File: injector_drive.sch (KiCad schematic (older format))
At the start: 10 parts

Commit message: Corrected ERC errors by fixing the custom FreeEMS components pinouts
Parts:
- removed R?: 1k, R4-SM0805, symbol R
- added R124: 1k, R4-SM0805, symbol R
- gave numbers to parts that had none: 9
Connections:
- net inductive_power_drive: now also R124.2
- net at U15.1 (IN): now also R124.1
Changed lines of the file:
@@
-EESchema Schematic File Version 2  date Sat 03 Jul 2010 10:49:02 AM ART
+EESchema Schematic File Version 2  date Sat 03 Jul 2010 12:32:24 PM ART
 LIBS:power
 LIBS:freeEMS_lib
@@
 Rsense MUST BE KELVIN CONNECTED TO THE DEVICE PINS
 $Comp
-L GND #PWR?
+L GND #PWR021
 U 1 1 4C2ED38A
 P 6600 2750
-AR Path="/4C2F3BE4/4C2ED38A" Ref="#PWR?"  Part="1"
-AR Path="/4C2F3DD9/4C2ED38A" Ref="#PWR?"  Part="1"
-F 0 "#PWR?" H 6600 2750 30  0001 C CNN
+AR Path="/4C2F3E4C/4C2ED38A" Ref="#PWR021"  Part="1"
+AR Path="/4C2F3E39/4C2ED38A" Ref="#PWR024"  Part="1"
+AR Path="/4C2F3E27/4C2ED38A" Ref="#PWR027"  Part="1"
+AR Path="/4C2F3E07/4C2ED38A" Ref="#PWR030"  Part="1"
+AR Path="/4C2F3DD9/4C2ED38A" Ref="#PWR033"  Part="1"
+AR Path="/4C2F3BE4/4C2ED38A" Ref="#PWR036"  Part="1"
+F 0 "#PWR036" H 6600 2750 30  0001 C CNN
 F 1 "GND" H 6600 2680 30  0001 C CNN
 	1    6600 2750
@@
 $EndComp
 $Comp
-L GND #PWR?
+L GND #PWR022
 U 1 1 4C2ED35A
 P 5950 3650
-AR Path="/4C2F3BE4/4C2ED35A" Ref="#PWR?"  Part="1"
-AR Path="/4C2F3DD9/4C2ED35A" Ref="#PWR?"  Part="1"
-F 0 "#PWR?" H 5950 3650 30  0001 C CNN
+AR Path="/4C2F3E4C/4C2ED35A" Ref="#PWR022"  Part="1"
+AR Path="/4C2F3E39/4C2ED35A" Ref="#PWR025"  Part="1"
+AR Path="/4C2F3E27/4C2ED35A" Ref="#PWR028"  Part="1"
+AR Path="/4C2F3E07/4C2ED35A" Ref="#PWR031"  Part="1"
+AR Path="/4C2F3DD9/4C2ED35A" Ref="#PWR034"  Part="1"
+AR Path="/4C2F3BE4/4C2ED35A" Ref="#PWR037"  Part="1"
+F 0 "#PWR037" H 5950 3650 30  0001 C CNN
 F 1 "GND" H 5950 3580 30  0001 C CNN
 	1    5950 3650
@@
 $EndComp
 $Comp
-L GND #PWR?
+L GND #PWR023
 U 1 1 4C2ED354
 P 6100 3000
-AR Path="/4C2F3BE4/4C2ED354" Ref="#PWR?"  Part="1"
-AR Path="/4C2F3DD9/4C2ED354" Ref="#PWR?"  Part="1"
-F 0 "#PWR?" H 6100 3000 30  0001 C CNN
+AR Path="/4C2F3E4C/4C2ED354" Ref="#PWR023"  Part="1"
+AR Path="/4C2F3E39/4C2ED354" Ref="#PWR026"  Part="1"
+AR Path="/4C2F3E27/4C2ED354" Ref="#PWR029"  Part="1"
+AR Path="/4C2F3E07/4C2ED354" Ref="#PWR032"  Part="1"
+AR Path="/4C2F3DD9/4C2ED354" Ref="#PWR035"  Part="1"
+AR Path="/4C2F3BE4/4C2ED354" Ref="#PWR038"  Part="1"
+F 0 "#PWR038" H 6100 3000 30  0001 C CNN
 F 1 "GND" H 6100 2930 30  0001 C CNN
 	1    6100 3000
@@
 $EndComp
 $Comp
-L C C?
+L C C59
 U 1 1 4C2ED144
 P 6600 2550
-AR Path="/4C2F3BE4/4C2ED144" Ref="C?"  Part="1"
-AR Path="/4C2F3DD9/4C2ED144" Ref="C?"  Part="1"
-F 0 "C?" H 6650 2650 50  0000 L CNN
+AR Path="/4C2F3E4C/4C2ED144" Ref="C59"  Part="1"
+AR Path="/4C2F3E39/4C2ED144" Ref="C57"  Part="1"
+AR Path="/4C2F3E27/4C2ED144" Ref="C55"  Part="1"
+AR Path="/4C2F3E07/4C2ED144" Ref="C53"  Part="1"
+AR Path="/4C2F3DD9/4C2ED144" Ref="C51"  Part="1"
+AR Path="/4C2F3BE4/4C2ED144" Ref="C49"  Part="1"
+F 0 "C59" H 6650 2650 50  0000 L CNN
 F 1 "1uF" H 6650 2450 50  0000 L CNN
 	1    6600 2550
@@
 $EndComp
 $Comp
-L R R?
+L R R126
 U 1 1 4C2ED135
 P 6250 2550
-AR Path="/4C2F3BE4/4C2ED135" Ref="R?"  Part="1"
-AR Path="/4C2F3DD9/4C2ED135" Ref="R?"  Part="1"
-F 0 "R?" V 6330 2550 50  0000 C CNN
+AR Path="/4C2F3E4C/4C2ED135" Ref="R126"  Part="1"
+AR Path="/4C2F3E39/4C2ED135" Ref="R123"  Part="1"
+AR Path="/4C2F3E27/4C2ED135" Ref="R120"  Part="1"
+AR Path="/4C2F3E07/4C2ED135" Ref="R117"  Part="1"
+AR Path="/4C2F3DD9/4C2ED135" Ref="R114"  Part="1"
+AR Path="/4C2F3BE4/4C2ED135" Ref="R111"  Part="1"
+F 0 "R126" V 6330 2550 50  0000 C CNN
 F 1 "3.9k" V 6250 2550 50  0000 C CNN
 	1    6250 2550
@@
 $EndComp
 $Comp
-L ZENER D?
+L ZENER D57
 U 1 1 4C2ED0C2
 P 3150 3150
-AR Path="/4C2F3BE4/4C2ED0C2" Ref="D?"  Part="1"
-AR Path="/4C2F3DD9/4C2ED0C2" Ref="D?"  Part="1"
-F 0 "D?" H 3150 3250 50  0000 C CNN
+AR Path="/4C2F3E4C/4C2ED0C2" Ref="D57"  Part="1"
+AR Path="/4C2F3E39/4C2ED0C2" Ref="D56"  Part="1"
+AR Path="/4C2F3E27/4C2ED0C2" Ref="D55"  Part="1"
+AR Path="/4C2F3E07/4C2ED0C2" Ref="D54"  Part="1"
+AR Path="/4C2F3DD9/4C2ED0C2" Ref="D53"  Part="1"
+AR Path="/4C2F3BE4/4C2ED0C2" Ref="D52"  Part="1"
+F 0 "D57" H 3150 3250 50  0000 C CNN
 F 1 "33v 5w" H 3150 3050 40  0000 C CNN
 	1    3150 3150
@@
 $EndComp
 $Comp
-L R R?
+L R R125
 U 1 1 4C2ED077
 P 5200 3450
-AR Path="/4C2F3BE4/4C2ED077" Ref="R?"  Part="1"
-AR Path="/4C2F3DD9/4C2ED077" Ref="R?"  Part="1"
-F 0 "R?" V 5280 3450 50  0000 C CNN
+AR Path="/4C2F3E4C/4C2ED077" Ref="R125"  Part="1"
+AR Path="/4C2F3E39/4C2ED077" Ref="R122"  Part="1"
+AR Path="/4C2F3E27/4C2ED077" Ref="R119"  Part="1"
+AR Path="/4C2F3E07/4C2ED077" Ref="R116"  Part="1"
+AR Path="/4C2F3DD9/4C2ED077" Ref="R113"  Part="1"
+AR Path="/4C2F3BE4/4C2ED077" Ref="R110"  Part="1"
+F 0 "R125" V 5280 3450 50  0000 C CNN
 F 1 "0.1 2W" V 5200 3450 50  0000 C CNN
 	1    5200 3450
@@
 $EndComp
 $Comp
-L C C?
+L C C58
 U 1 1 4C2ED01B
 P 4150 3000
-AR Path="/4C2F3BE4/4C2ED01B" Ref="C?"  Part="1"
-AR Path="/4C2F3DD9/4C2ED01B" Ref="C?"  Part="1"
-F 0 "C?" H 4200 3100 50  0000 L CNN
+AR Path="/4C2F3E4C/4C2ED01B" Ref="C58"  Part="1"
+AR Path="/4C2F3E39/4C2ED01B" Ref="C56"  Part="1"
+AR Path="/4C2F3E27/4C2ED01B" Ref="C54"  Part="1"
+AR Path="/4C2F3E07/4C2ED01B" Ref="C52"  Part="1"
+AR Path="/4C2F3DD9/4C2ED01B" Ref="C50"  Part="1"
+AR Path="/4C2F3BE4/4C2ED01B" Ref="C48"  Part="1"
+F 0 "C58" H 4200 3100 50  0000 L CNN
 F 1 ".01uF" H 4200 2900 50  0000 L CNN
 	1    4150 3000
@@
 $EndComp
 $Comp
-L DARL_N Q?
+L DARL_N Q17
 U 1 1 4C2ECF62
 P 3600 3200
-AR Path="/4C2F3BE4/4C2ECF62" Ref="Q?"  Part="1"
-AR Path="/4C2F3DD9/4C2ECF62" Ref="Q?"  Part="1"
-F 0 "Q?" H 3600 3450 50  0000 C CNN
+AR Path="/4C2F3E4C/4C2ECF62" Ref="Q17"  Part="1"
+AR Path="/4C2F3E39/4C2ECF62" Ref="Q16"  Part="1"
+AR Path="/4C2F3E27/4C2ECF62" Ref="Q15"  Part="1"
+AR Path="/4C2F3E07/4C2ECF62" Ref="Q14"  Part="1"
+AR Path="/4C2F3DD9/4C2ECF62" Ref="Q13"  Part="1"
+AR Path="/4C2F3BE4/4C2ECF62" Ref="Q12"  Part="1"
+F 0 "Q17" H 3600 3450 50  0000 C CNN
 F 1 "2N6044" H 3400 3100 50  0000 C CNN
 	1    3600 3200
@@
 $EndComp
 $Comp
-L LM1949 U?
+L LM1949 U15
 U 1 1 4C2ECEC5
 P 5150 2850
-AR Path="/4C2F3BE4/4C2ECEC5" Ref="U?"  Part="1"
-AR Path="/4C2F3DD9/4C2ECEC5" Ref="U?"  Part="1"
-F 0 "U?" H 5200 3150 60  0000 C CNN
+AR Path="/4C2F3E4C/4C2ECEC5" Ref="U15"  Part="1"
+AR Path="/4C2F3E39/4C2ECEC5" Ref="U14"  Part="1"
+AR Path="/4C2F3E27/4C2ECEC5" Ref="U13"  Part="1"
+AR Path="/4C2F3E07/4C2ECEC5" Ref="U12"  Part="1"
+AR Path="/4C2F3DD9/4C2ECEC5" Ref="U11"  Part="1"
+AR Path="/4C2F3BE4/4C2ECEC5" Ref="U10"  Part="1"
+F 0 "U15" H 5200 3150 60  0000 C CNN
 F 1 "LM1949" H 5150 2500 60  0000 C CNN
 F 2 "DIP8" H 5260 3210 60  0001 C CNN
@@
 $EndComp
 $Comp
-L CONN_1 P?
+L CONN_1 P55
 U 1 1 48AA1A76
 P 3650 2700
-AR Path="/4C2F3BE4/48AA1A76" Ref="P?"  Part="1"
-AR Path="/4C2F3DD9/48AA1A76" Ref="P?"  Part="1"
-F 0 "P?" H 3730 2700 40  0000 L CNN
+AR Path="/4C2F3E4C/48AA1A76" Ref="P55"  Part="1"
+AR Path="/4C2F3E39/48AA1A76" Ref="P53"  Part="1"
+AR Path="/4C2F3E27/48AA1A76" Ref="P51"  Part="1"
+AR Path="/4C2F3E07/48AA1A76" Ref="P49"  Part="1"
+AR Path="/4C2F3DD9/48AA1A76" Ref="P47"  Part="1"
+AR Path="/4C2F3BE4/48AA1A76" Ref="P45"  Part="1"
+F 0 "P55" H 3730 2700 40  0000 L CNN
 F 1 "CONN_1" H 3650 2755 30  0001 C CNN
 F 2 "1PIN" V -2870 3300 60  0001 C CNN
@@
 $EndComp
 $Comp
-L CONN_1 P?
+L CONN_1 P54
 U 1 1 48AA1A73
 P 3650 2500
-AR Path="/4C2F3BE4/48AA1A73" Ref="P?"  Part="1"
-AR Path="/4C2F3DD9/48AA1A73" Ref="P?"  Part="1"
-F 0 "P?" H 3730 2500 40  0000 L CNN
+AR Path="/4C2F3E4C/48AA1A73" Ref="P54"  Part="1"
+AR Path="/4C2F3E39/48AA1A73" Ref="P52"  Part="1"
+AR Path="/4C2F3E27/48AA1A73" Ref="P50"  Part="1"
+AR Path="/4C2F3E07/48AA1A73" Ref="P48"  Part="1"
+AR Path="/4C2F3DD9/48AA1A73" Ref="P46"  Part="1"
+AR Path="/4C2F3BE4/48AA1A73" Ref="P44"  Part="1"
+F 0 "P54" H 3730 2500 40  0000 L CNN
 F 1 "CONN_1" H 3650 2555 30  0001 C CNN
 F 2 "1PIN" V -2870 3300 60  0001 C CNN
@@
 12v_power
 $Comp
-L R R?
-U 1 1 488A2B3B
+L R R124
+U 1 1 4C2F52D2
 P 3600 2000
-AR Path="/4C2F3BE4/488A2B3B" Ref="R?"  Part="1"
-AR Path="/4C2F3DD9/488A2B3B" Ref="R?"  Part="1"
-F 0 "R?" V 3680 2000 50  0000 C CNN
+AR Path="/4C2F3E4C/4C2F52D2" Ref="R124"  Part="1"
+AR Path="/4C2F3E39/4C2F52D2" Ref="R121"  Part="1"
+AR Path="/4C2F3E27/4C2F52D2" Ref="R118"  Part="1"
+AR Path="/4C2F3E07/4C2F52D2" Ref="R115"  Part="1"
+AR Path="/4C2F3DD9/4C2F52D2" Ref="R112"  Part="1"
+AR Path="/4C2F3BE4/4C2F52D2" Ref="R109"  Part="1"
+F 0 "R124" V 3680 2000 50  0000 C CNN
 F 1 "1k" V 3600 2000 50  0000 C CNN
 F 2 "R4-SM0805" V 3780 2100 60  0001 C CNN

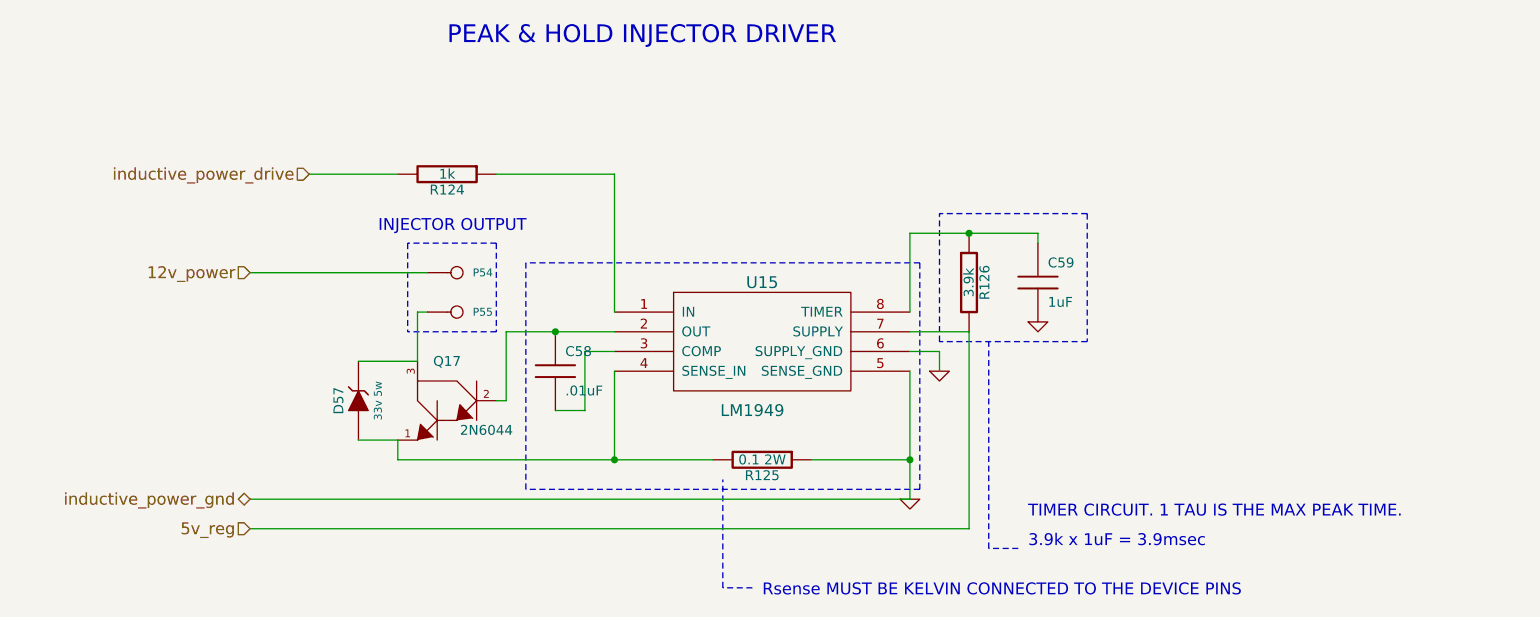
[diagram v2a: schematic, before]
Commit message: PCB redesign. Only P&H is layeed down.
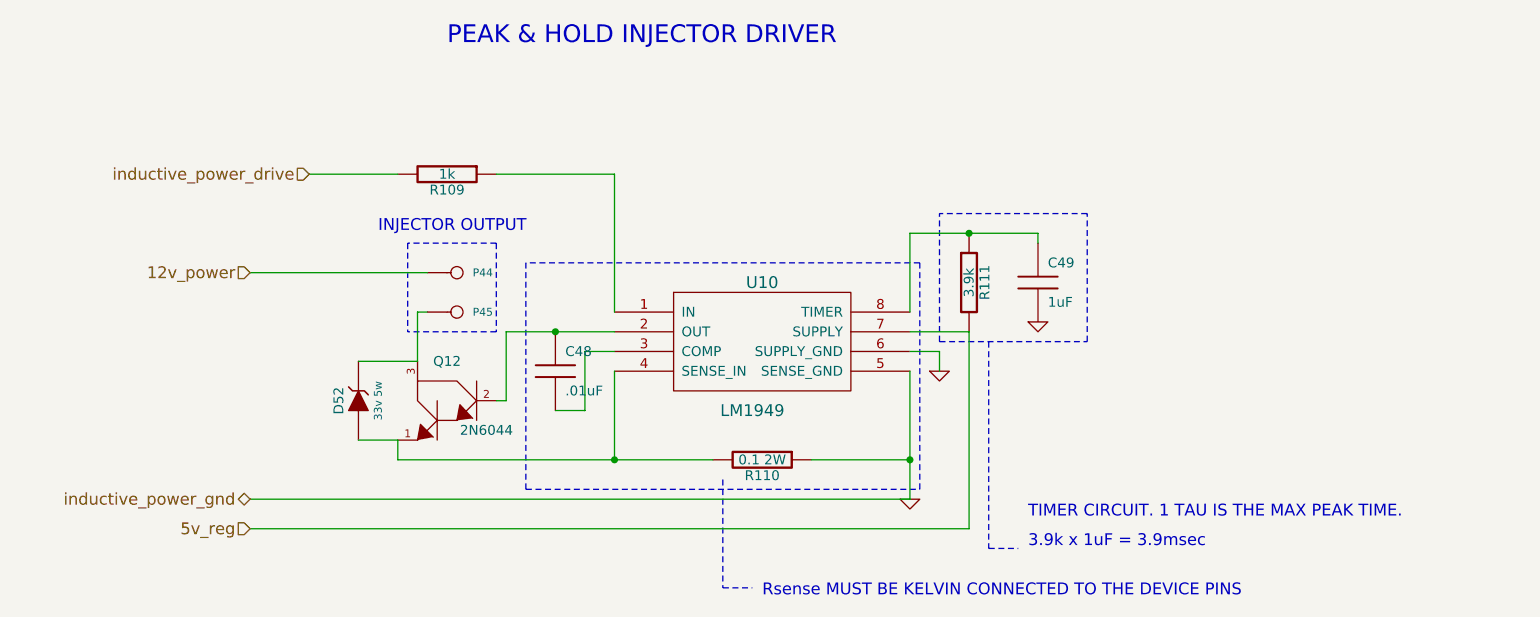
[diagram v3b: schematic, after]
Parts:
- U15: footprint DIP8 -> 8dip300
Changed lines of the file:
@@
-EESchema Schematic File Version 2  date Sat 03 Jul 2010 12:32:24 PM ART
+EESchema Schematic File Version 2  date Sat 03 Jul 2010 05:37:07 PM ART
 LIBS:power
 LIBS:freeEMS_lib
@@
 EELAYER END
 $Descr A4 11700 8267
-Sheet 2 41
+Sheet 7 41
 Title "freeEMS 1.0"
 Date "3 jul 2010"
@@
 Comment4 ""
 $EndDescr
+Wire Wire Line
+	3350 2000 2900 2000
+Wire Notes Line
+	5000 3550 5000 4100
+Wire Notes Line
+	5000 4100 5150 4100
+Wire Notes Line
+	3850 2800 3400 2800
+Wire Notes Line
+	3850 2350 3400 2350
+Wire Notes Line
+	3850 2350 3850 2800
+Wire Notes Line
+	3400 2350 3400 2800
+Wire Wire Line
+	2600 3800 6250 3800
+Wire Wire Line
+	6250 3800 6250 2800
+Wire Wire Line
+	6100 3000 6100 2900
+Wire Wire Line
+	6100 2900 5950 2900
+Connection ~ 6250 2300
+Wire Wire Line
+	6600 2350 6600 2300
+Wire Wire Line
+	6600 2300 5950 2300
+Wire Wire Line
+	4450 2700 4450 2000
+Wire Wire Line
+	4450 2000 3850 2000
+Wire Wire Line
+	2600 2500 3500 2500
+Wire Wire Line
+	3150 2950 3450 2950
+Connection ~ 4450 3450
+Wire Wire Line
+	3350 3450 3350 3350
+Wire Wire Line
+	3350 3450 4950 3450
+Wire Wire Line
+	5450 3450 5950 3450
+Wire Wire Line
+	3900 3150 3900 2800
+Wire Wire Line
+	3900 3150 3850 3150
+Wire Wire Line
+	3900 2800 4450 2800
+Connection ~ 4150 2800
+Wire Wire Line
+	4150 3200 4300 3200
+Wire Wire Line
+	4300 3200 4300 2900
+Wire Wire Line
+	4300 2900 4450 2900
+Wire Wire Line
+	4450 3450 4450 3000
+Wire Wire Line
+	3350 3350 3150 3350
+Wire Wire Line
+	3450 2950 3450 2700
+Wire Wire Line
+	3450 2700 3500 2700
+Wire Wire Line
+	5950 2300 5950 2700
+Wire Wire Line
+	6250 2800 5950 2800
+Wire Wire Line
+	2600 3650 5950 3650
+Wire Wire Line
+	5950 3650 5950 3000
+Connection ~ 5950 3450
+Wire Notes Line
+	6100 2850 6100 2200
+Wire Notes Line
+	6100 2850 6850 2850
+Wire Notes Line
+	6850 2850 6850 2200
+Wire Notes Line
+	6850 2200 6100 2200
+Wire Notes Line
+	4000 3600 4000 2450
+Wire Notes Line
+	4000 3600 6000 3600
+Wire Notes Line
+	6000 3600 6000 2450
+Wire Notes Line
+	6000 2450 4000 2450
+Wire Notes Line
+	6350 2850 6350 3900
+Wire Notes Line
+	6350 3900 6500 3900
 Text Notes 3600 1350 0    90   ~ 0
 PEAK & HOLD INJECTOR DRIVER
@@
 Text Notes 3250 2300 0    60   ~ 0
 INJECTOR OUTPUT
-Wire Notes Line
-	6500 3900 6350 3900
-Wire Notes Line
-	6350 3900 6350 2850
-Wire Notes Line
-	6000 2450 4000 2450
-Wire Notes Line
-	6000 2450 6000 3600
-Wire Notes Line
-	6000 3600 4000 3600
-Wire Notes Line
-	4000 3600 4000 2450
-Wire Notes Line
-	6850 2200 6100 2200
-Wire Notes Line
-	6850 2200 6850 2850
-Wire Notes Line
-	6850 2850 6100 2850
-Wire Notes Line
-	6100 2850 6100 2200
-Connection ~ 5950 3450
-Wire Wire Line
-	5950 3000 5950 3650
-Wire Wire Line
-	5950 3650 2600 3650
-Wire Wire Line
-	5950 2800 6250 2800
-Wire Wire Line
-	5950 2700 5950 2300
-Wire Wire Line
-	2900 2000 3350 2000
-Wire Wire Line
-	3500 2700 3450 2700
-Wire Wire Line
-	3450 2700 3450 2950
-Wire Wire Line
-	3150 3350 3350 3350
-Wire Wire Line
-	4450 3450 4450 3000
-Wire Wire Line
-	4450 2900 4300 2900
-Wire Wire Line
-	4300 2900 4300 3200
-Wire Wire Line
-	4300 3200 4150 3200
-Connection ~ 4150 2800
-Wire Wire Line
-	4450 2800 3900 2800
-Wire Wire Line
-	3850 3150 3900 3150
-Wire Wire Line
-	3900 3150 3900 2800
-Wire Wire Line
-	5450 3450 5950 3450
-Wire Wire Line
-	4950 3450 3350 3450
-Wire Wire Line
-	3350 3450 3350 3350
-Connection ~ 4450 3450
-Wire Wire Line
-	3450 2950 3150 2950
-Wire Wire Line
-	2600 2500 3500 2500
-Wire Wire Line
-	3850 2000 4450 2000
-Wire Wire Line
-	4450 2000 4450 2700
-Wire Wire Line
-	5950 2300 6600 2300
-Wire Wire Line
-	6600 2300 6600 2350
-Connection ~ 6250 2300
-Wire Wire Line
-	5950 2900 6100 2900
-Wire Wire Line
-	6100 2900 6100 3000
-Wire Wire Line
-	6250 2800 6250 3800
-Wire Wire Line
-	6250 3800 2600 3800
-Wire Notes Line
-	3400 2350 3400 2800
-Wire Notes Line
-	3850 2350 3850 2800
-Wire Notes Line
-	3850 2350 3400 2350
-Wire Notes Line
-	3850 2800 3400 2800
-Wire Notes Line
-	5150 4100 5000 4100
-Wire Notes Line
-	5000 4100 5000 3550
 Text Notes 6550 3750 0    60   ~ 0
 TIMER CIRCUIT. 1 TAU IS THE MAX PEAK TIME.
@@
 AR Path="/4C2F3DD9/4C2ED144" Ref="C51"  Part="1"
 AR Path="/4C2F3BE4/4C2ED144" Ref="C49"  Part="1"
-F 0 "C59" H 6650 2650 50  0000 L CNN
+F 0 "C49" H 6650 2650 50  0000 L CNN
 F 1 "1uF" H 6650 2450 50  0000 L CNN
 	1    6600 2550
@@
 AR Path="/4C2F3DD9/4C2ED135" Ref="R114"  Part="1"
 AR Path="/4C2F3BE4/4C2ED135" Ref="R111"  Part="1"
-F 0 "R126" V 6330 2550 50  0000 C CNN
+F 0 "R111" V 6330 2550 50  0000 C CNN
 F 1 "3.9k" V 6250 2550 50  0000 C CNN
 	1    6250 2550
@@
 AR Path="/4C2F3DD9/4C2ED0C2" Ref="D53"  Part="1"
 AR Path="/4C2F3BE4/4C2ED0C2" Ref="D52"  Part="1"
-F 0 "D57" H 3150 3250 50  0000 C CNN
+F 0 "D52" H 3150 3250 50  0000 C CNN
 F 1 "33v 5w" H 3150 3050 40  0000 C CNN
 	1    3150 3150
@@
 AR Path="/4C2F3DD9/4C2ED077" Ref="R113"  Part="1"
 AR Path="/4C2F3BE4/4C2ED077" Ref="R110"  Part="1"
-F 0 "R125" V 5280 3450 50  0000 C CNN
+F 0 "R110" V 5280 3450 50  0000 C CNN
 F 1 "0.1 2W" V 5200 3450 50  0000 C CNN
 	1    5200 3450
@@
 AR Path="/4C2F3DD9/4C2ED01B" Ref="C50"  Part="1"
 AR Path="/4C2F3BE4/4C2ED01B" Ref="C48"  Part="1"
-F 0 "C58" H 4200 3100 50  0000 L CNN
+F 0 "C48" H 4200 3100 50  0000 L CNN
 F 1 ".01uF" H 4200 2900 50  0000 L CNN
 	1    4150 3000
@@
 AR Path="/4C2F3DD9/4C2ECF62" Ref="Q13"  Part="1"
 AR Path="/4C2F3BE4/4C2ECF62" Ref="Q12"  Part="1"
-F 0 "Q17" H 3600 3450 50  0000 C CNN
+F 0 "Q12" H 3600 3450 50  0000 C CNN
 F 1 "2N6044" H 3400 3100 50  0000 C CNN
 	1    3600 3200
@@
 AR Path="/4C2F3DD9/4C2ECEC5" Ref="U11"  Part="1"
 AR Path="/4C2F3BE4/4C2ECEC5" Ref="U10"  Part="1"
-F 0 "U15" H 5200 3150 60  0000 C CNN
+F 0 "U10" H 5200 3150 60  0000 C CNN
 F 1 "LM1949" H 5150 2500 60  0000 C CNN
-F 2 "DIP8" H 5260 3210 60  0001 C CNN
+F 2 "8dip300" H 5260 3210 60  0001 C CNN
 	1    5150 2850
 	1    0    0    -1
@@
 AR Path="/4C2F3DD9/48AA1A76" Ref="P47"  Part="1"
 AR Path="/4C2F3BE4/48AA1A76" Ref="P45"  Part="1"
-F 0 "P55" H 3730 2700 40  0000 L CNN
+F 0 "P45" H 3730 2700 40  0000 L CNN
 F 1 "CONN_1" H 3650 2755 30  0001 C CNN
 F 2 "1PIN" V -2870 3300 60  0001 C CNN
@@
 AR Path="/4C2F3DD9/48AA1A73" Ref="P46"  Part="1"
 AR Path="/4C2F3BE4/48AA1A73" Ref="P44"  Part="1"
-F 0 "P54" H 3730 2500 40  0000 L CNN
+F 0 "P44" H 3730 2500 40  0000 L CNN
 F 1 "CONN_1" H 3650 2555 30  0001 C CNN
 F 2 "1PIN" V -2870 3300 60  0001 C CNN
@@
 AR Path="/4C2F3DD9/4C2F52D2" Ref="R112"  Part="1"
 AR Path="/4C2F3BE4/4C2F52D2" Ref="R109"  Part="1"
-F 0 "R124" V 3680 2000 50  0000 C CNN
+F 0 "R109" V 3680 2000 50  0000 C CNN
 F 1 "1k" V 3600 2000 50  0000 C CNN
 F 2 "R4-SM0805" V 3780 2100 60  0001 C CNN
